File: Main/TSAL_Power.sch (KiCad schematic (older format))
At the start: 122 parts, among them Q10 NPN, Q11 MJD122, Q12 PNP, Q6 BSC0904NSI, Q7 BSC0902NSI, Q8 BSC0902NSI, Q9 MJD122, U10 TLV431, U11 TLV431, U4 TPS562200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

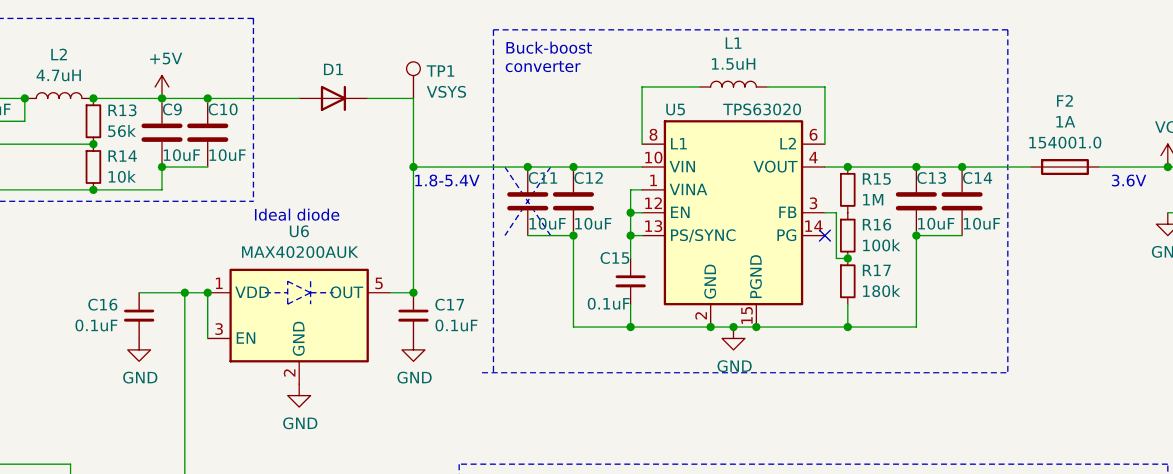
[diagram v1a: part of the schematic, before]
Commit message: increase output filter capacitor value
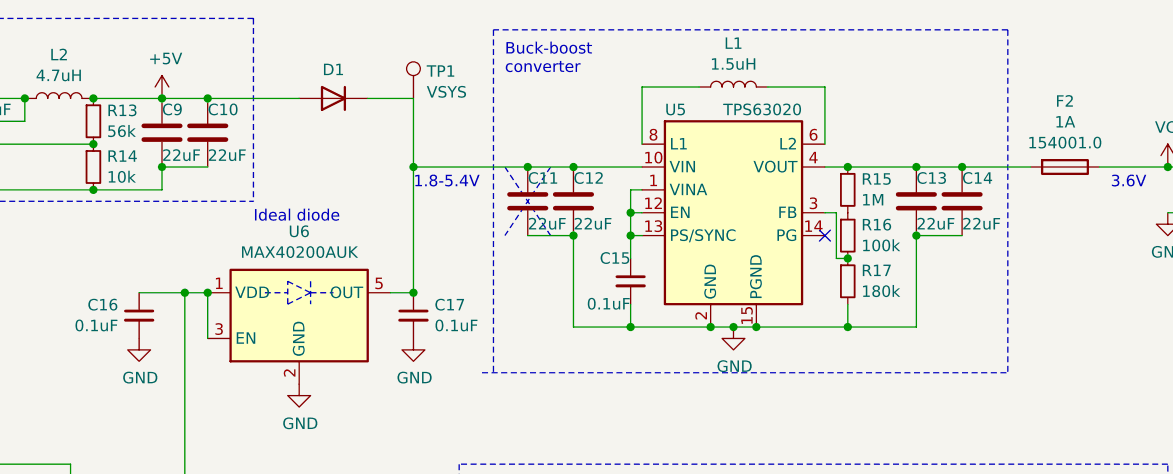
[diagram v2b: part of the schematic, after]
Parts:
- C10, C11, C12, C13, C14, C9: value 10uF -> 22uF
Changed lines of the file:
@@
 P 9400 1950
 F 0 "C13" H 9400 2050 50  0000 L CNN
-F 1 "10uF" H 9400 1850 50  0000 L CNN
+F 1 "22uF" H 9400 1850 50  0000 L CNN
 F 2 "archive:C_0805_2012Metric" H 9438 1800 50  0001 C CNN
 F 3 "~" H 9400 1950 50  0001 C CNN
@@
 P 9600 1950
 F 0 "C14" H 9600 2050 50  0000 L CNN
-F 1 "10uF" H 9600 1850 50  0000 L CNN
+F 1 "22uF" H 9600 1850 50  0000 L CNN
 F 2 "archive:C_0805_2012Metric" H 9638 1800 50  0001 C CNN
 F 3 "~" H 9600 1950 50  0001 C CNN
@@
 P 6300 1650
 F 0 "C10" H 6300 1750 50  0000 L CNN
-F 1 "10uF" H 6300 1550 50  0000 L CNN
+F 1 "22uF" H 6300 1550 50  0000 L CNN
 F 2 "archive:C_0805_2012Metric" H 6338 1500 50  0001 C CNN
 F 3 "~" H 6300 1650 50  0001 C CNN
@@
 P 6100 1650
 F 0 "C9" H 6100 1750 50  0000 L CNN
-F 1 "10uF" H 6100 1550 50  0000 L CNN
+F 1 "22uF" H 6100 1550 50  0000 L CNN
 F 2 "archive:C_0805_2012Metric" H 6138 1500 50  0001 C CNN
 F 3 "~" H 6100 1650 50  0001 C CNN
@@
 P 7700 1950
 F 0 "C11" H 7700 2050 50  0000 L CNN
-F 1 "10uF" H 7700 1850 50  0000 L CNN
+F 1 "22uF" H 7700 1850 50  0000 L CNN
 F 2 "archive:C_0805_2012Metric" H 7738 1800 50  0001 C CNN
 F 3 "~" H 7700 1950 50  0001 C CNN
@@
 P 7900 1950
 F 0 "C12" H 7900 2050 50  0000 L CNN
-F 1 "10uF" H 7900 1850 50  0000 L CNN
+F 1 "22uF" H 7900 1850 50  0000 L CNN
 F 2 "archive:C_0805_2012Metric" H 7938 1800 50  0001 C CNN
 F 3 "~" H 7900 1950 50  0001 C CNN
